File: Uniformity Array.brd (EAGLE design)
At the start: 43.2 x 34.3 mm, 38 parts, among them IC1 SI1145, J3 USB-MICRO!!!, J4 3x2M, Q1 200mA/50V, Q2 200mA/50V, U1 ATMEGA32U4-TQFP44, U2 ATMEGA32U4-TQFP44, U4 LP2985-33DBVR, Y3 16MHz KX-7

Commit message: schematiced
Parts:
- removed C8: 1uF, SmartPrj:C0402
- removed IC1: SI1145, silabs:QFN-10
- removed L2: MH2029-300Y, wuerth-elektronik:0805
- removed Q1, Q2: 200mA/50V, SparkFun-DiscreteSemi:SOT23-3
- removed R3, R6, R9: (no value), arduino-micro-reference-designArduino_Micro_Rev03j:SMARTPRJ_R0402
- removed R7: (no value), arduino-micro-reference-designArduino_Micro_Rev03j:SMARTPRJ_R0603-ROUND
- removed RESET: TS42, SmartPrj:TS42
- removed RP3: 22R, resistor-dil:CAY16
- removed Y3: 16MHz KX-7, SmartPrj:CRYSTAL-3.2-2.5
- added C1, C15, C16, C17, C18, C19, C2, C20, C21, C22, C23, C24, C25, C26, C27, C28, C29, C3, C30, C31, C32, C33, C34: 1uf, Seeed-Capacitor-2016:C0402
- added IC10, IC11, IC12, IC13, IC14, IC15, IC16, IC17, IC18, IC19, IC2, IC20, IC21, IC3, IC4, IC5, IC6, IC7, IC8, IC9: SI1145, silabs:QFN-10
- added K1: DTSM-62K-S-V-T/R, Seeed-Switch-2016:SW4-SMD-6.0X6.0X5.0MM
- added L1: 330R-1500MA, Seeed-OPL-Inductor:L0805
- added R10: 10K, Seeed-OPL-Resistor:R0402
- added R11: 22R, Seeed-Resistor-2016:R0603
- added R12, R13, R14, R15, R16, R17, R18, R19, R20, R21, R22, R23, R24, R25, R26, R27, R28, R29, R30, R31, R32, R33, R34, R35, R36, R37, R38, R39, R40, R41, R42, R43, R44, R45, R46, R47, R48, R49, R50, R51, R52, R53: 510R, Seeed-Resistor-2016:R0603
- added U3, U5: PCA9547D,112, NXP_By_element14_Batch_1:SOIC127P1032X265-24N
- added Y1: 16MHZ, Seeed-Crystal Oscillator-2016:X2-SMD-5.0X3.2X1.3MM
- C10, C11, C6, C9: value 100n -> 100nf; device SmartPrj:C0402 -> Seeed-Capacitor-2016:C0402
- C12: value 22pF -> 10pf; device SmartPrj:C0402 -> Seeed-Capacitor-2016:C0603
- C13: value 22pF -> 4.7PF; device SmartPrj:C0402 -> Seeed-Capacitor-2016:C0603
- C14: value 22u -> 22uf; device rcl:SMC_B -> Seeed-Capacitor-2016:AVX-A
- C4, C7: value 1uF -> 1uf; device SmartPrj:C0402 -> Seeed-Capacitor-2016:C0402
- C5: value 1uF -> 1uf; device arduino-micro-reference-designArduino_Micro_Rev03j:SMARTPRJ_C0603-ROUND -> Seeed-Capacitor-2016:C0402
- D2: value CD1206-S01575 -> 75V 150MA; device diode:MINIMELF -> Seeed-Diode-2016:LED-1206
- F1: value MF-MSMF050-2 500mA -> MF-MSMF050-2; device rcl:L1812 -> Seeed-Fuse-2016:F1812
- J4: value 3x2M -> 2x3p-2.54; device SmartPrj:2X03 -> Seeed-Connector -2016:H2X3-2.54
- L: value green -> GREEN-0805; device led:CHIPLED_0805 -> Seeed-LED-2016:LED-0805
- ON: value blue -> CLEAR-BLUE-0805; device led:CHIPLED_0805 -> Seeed-LED-2016:LED-0805
- R1, R2, R5, R8: device SmartPrj:R0402 -> Seeed-Resistor-2016:R0402
- R4: value 10K -> 22R; device SmartPrj:R0402 -> Seeed-Resistor-2016:R0603
- U2: value ATMEGA32U4-TQFP44 -> PCA9547D,112; device Seeed-OPL-ic:TQFP44-0.8-9.6X9.6MM -> NXP_By_element14_Batch_1:SOIC127P1032X265-24N
- U4: device SmartPrj:SOT23-DBV -> Seeed-IC-2016:SOT-23-5
- Z1, Z2: value CG0603MLC-05E -> 5V-28V; device varistor:CT/CN0603 -> Seeed-Diode-2016:R0603
- moved U2 65.1 mm to (52.1, 26.7), turned to 90 degrees
- moved R4 57.5 mm to (-6.35, -22.9), turned to 0 degrees
- moved U4 6.35 mm to (27.9, 33.0)
- moved C11 5.08 mm to (24.1, 29.2)
- moved R2 3.81 mm to (15.2, 31.8)
- moved R5 3.81 mm to (15.2, 34.3)
- moved ON 2.84 mm to (19.8, 33.4)
- moved C14 2.54 mm to (3.81, 30.9)
- moved C4 2.54 mm to (31.8, 29.2)
- moved C6 2.54 mm to (20.3, 27.7)
- moved C7 2.54 mm to (17.8, 27.7)
- moved C9 2.54 mm to (17.8, 30.5)
- moved F1 2.54 mm to (9.65, 31.0)
- moved U1 1.27 mm to (21.6, 20.3)
- moved J4 0.28 mm to (13.8, 9.65), turned to 90 degrees
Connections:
- removed net 5-GND: RESET.5
- removed net HWB: R4.1, U1.33
- removed net N$2: IC1.1, Q1.2, R3.1
- removed net N$4: IC1.2, Q2.2, R6.1
- new net N$10: IC8.1, R13.2, U2.4
- new net N$11: IC8.2, R35.2, U2.5
- new net N$12: IC3.1, R18.2, U2.15
- new net N$13: IC4.1, R19.2, U2.13
- new net N$14: IC4.2, R21.2, U2.14
- new net N$15: IC3.2, R20.2, U2.16
- new net N$16: IC9.1, R17.2, U2.8
- new net N$17: IC9.2, R15.2, U2.9
- new net N$18: IC6.1, R16.2, U2.10
- new net N$19: IC6.2, R14.2, U2.11
- new net N$20: IC5.1, R45.2, U2.17
- new net N$21: IC5.2, R47.2, U2.18
- new net N$22: IC2.1, R46.2, U2.20
- new net N$23: IC2.2, R44.2, U2.19
- new net N$24: IC11.1, R24.2, U5.6
- new net N$25: IC12.1, R25.2, U5.4
- new net N$26: IC12.2, R23.2, U5.5
- new net N$27: IC11.2, R22.2, U5.7
- new net N$28: IC13.1, R27.2, U5.8
- new net N$29: IC13.2, R29.2, U5.9
- new net N$30: IC10.1, R26.2, U5.10
- new net N$31: IC10.2, R28.2, U5.11
- new net N$32: IC15.1, R30.2, U5.15
- new net N$33: IC16.1, R31.2, U5.13
- new net N$34: IC16.2, R33.2, U5.14
- new net N$35: IC15.2, R32.2, U5.16
- new net N$36: IC17.1, R50.2, U5.17
- new net N$37: IC17.2, R48.2, U5.18
- new net N$38: IC14.1, R51.2, U5.19
- new net N$39: IC14.2, R49.2, U5.20
- new net N$40: IC19.1, R38.2, U3.6
- new net N$41: IC20.1, R39.2, U3.4
- new net N$42: IC20.2, R37.2, U3.5
- new net N$43: IC19.2, R36.2, U3.7
- new net N$44: IC21.1, R41.2, U3.8
- new net N$45: IC21.2, R43.2, U3.9
- new net N$46: IC18.1, R40.2, U3.10
- new net N$47: IC18.2, R42.2, U3.11
- new net N$52: U5.3
- new net N$53: U3.3
- new net N$59: U2.3
- new net N$6: R10.2, U1.33
- new net N$8: IC7.1, R12.2, U2.6
- new net N$9: IC7.2, R34.2, U2.7
- net 3V3: now also C15.1, C17.1, C18.1, C19.1, C2.1, C21.1, C22.1, C23.1, C25.1, C26.1, C27.1, C29.1, C3.1, C30.1, C31.1, C32.2, C33.2, C34.2, IC10.3, IC11.3, IC12.3, IC13.3, IC14.3, IC15.3, IC16.3, IC17.3, IC18.3, IC19.3, IC2.3, IC20.3, IC21.3, IC3.3, IC4.3, IC5.3, IC6.3, IC7.3, IC8.3, IC9.3, R12.1, R13.1, R14.1, R15.1, R16.1, R17.1, R18.1, R19.1, R20.1, R21.1, R22.1, R23.1, R24.1, R25.1, R26.1, R27.1, R28.1, R29.1, R30.1, R31.1, R32.1, R33.1, R34.1, R35.1, R36.1, R37.1, R38.1, R39.1, R40.1, R41.1, R42.1, R43.1, R44.1, R45.1, R46.1, R47.1, R48.1, R49.1, R50.1, R51.1, U2.24, U3.2, U3.24, U5.1, U5.24; no longer C8.1, IC1.3, Q1.1, Q2.1, R3.2, R6.2
- net A3: no longer U1.39
- net AVCC: now also L1.1; no longer L2.2
- net D+: now also R4.1; no longer RP3.8
- net D-: now also R11.1; no longer RP3.7
- net GND: now also C1.2, C15.2, C16.2, C17.2, C18.2, C19.2, C2.2, C20.2, C21.2, C22.2, C23.2, C24.2, C25.2, C26.2, C27.2, C28.2, C29.2, C3.2, C30.2, C31.2, C32.1, C33.1, C34.1, IC10.8, IC11.8, IC12.8, IC13.8, IC14.8, IC15.8, IC16.8, IC17.8, IC18.8, IC19.8, IC2.8, IC20.8, IC21.8, IC3.8, IC4.8, IC5.8, IC6.8, IC7.8, IC8.8, IC9.8, J4.4, K1.2, K1.3, L.-, ON.-, R10.1, U2.1, U2.12, U2.2, U2.21, U3.1, U3.12, U3.21, U5.12, U5.2, U5.21; no longer C8.2, IC1.8, J4.6, L.C, ON.C, R4.2, RESET.3, RESET.4, Y3.2, Y3.4
- net MOSI: now also J4.5; no longer J4.4
- net N$3: now also ON.+; no longer ON.A
- net N$7: now also L.+; no longer L.A
- net RD+: now also R4.2; no longer RP3.1
- net RD-: now also R11.2; no longer RP3.2
- net RESET: now also D2.+, J4.3, K1.4; no longer D2.A, J4.5, RESET.2
- net SCK: now also J4.2; no longer J4.3
- net SCL: now also R53.1, U2.22, U3.22, U5.22; no longer Q2.3, R7.1
- net SDA: now also R52.1, U2.23, U3.23, U5.23; no longer Q1.3, R9.1
- net VUSB: now also D2.-, J4.6, L1.2, R52.2, R53.2; no longer D2.C, J4.2, L2.1, R7.2, R9.2
- net XTAL1: now also Y1.2; no longer Y3.3
- net XTAL2: now also Y1.1; no longer Y3.1
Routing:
- net GND: track 95.6 -> 5.07 mm, vias 11 -> 0
- net VUSB: track 84.2 -> 0.00 mm, vias 2 -> 0
- net 3V3: track 38.5 -> 0.00 mm
- net RESET: track 28.2 -> 0.00 mm
- net SCL: track 15.0 -> 0.00 mm
- net SDA: track 14.0 -> 0.00 mm
- net VUSBD: track 12.6 -> 0.00 mm
- net MOSI: track 11.9 -> 0.00 mm
- net MISO: track 8.95 -> 0.00 mm
- net SCK: track 8.86 -> 0.00 mm
- net D+: track 7.77 -> 0.00 mm
- net N$4: track 7.74 -> 0.00 mm
- net D-: track 7.55 -> 0.00 mm
- net XTAL1: track 7.36 -> 0.00 mm
- net AVCC: track 6.68 -> 0.00 mm
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- removed copper zone on layer 16, net GND
- removed copper zone on layer 1, net N$5
- removed copper zone on layer 1, net VUSB
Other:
- board outline removed

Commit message: sensors placed
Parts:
- moved C32 523.3 mm to (91.4, 69.8)
- moved C33 510.3 mm to (66.0, 69.8)
- moved C34 500.9 mm to (45.7, 69.8)
- moved R52 492.8 mm to (25.4, 69.8)
- moved R53 492.8 mm to (20.3, 69.8)
- moved R50 469.3 mm to (77.5, 17.8), turned to 180 degrees
- moved R51 469.0 mm to (77.5, 12.7), turned to 180 degrees
- moved R42 466.9 mm to (90.2, 39.4)
- moved R43 466.9 mm to (90.2, 34.3)
- moved R48 454.9 mm to (77.5, 7.62), turned to 180 degrees
- moved R49 454.6 mm to (77.5, 2.54), turned to 180 degrees
- moved R40 451.3 mm to (90.2, 29.2)
- moved R41 451.3 mm to (90.2, 24.1)
- moved R44 434.3 mm to (53.3, 17.8), turned to 180 degrees
- moved R45 433.4 mm to (53.3, 12.7), turned to 180 degrees
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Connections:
- net 3V3: now also C1.1, C20.1, C24.1, C28.1
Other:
- board outline added: 102.9 x 81.3 mm

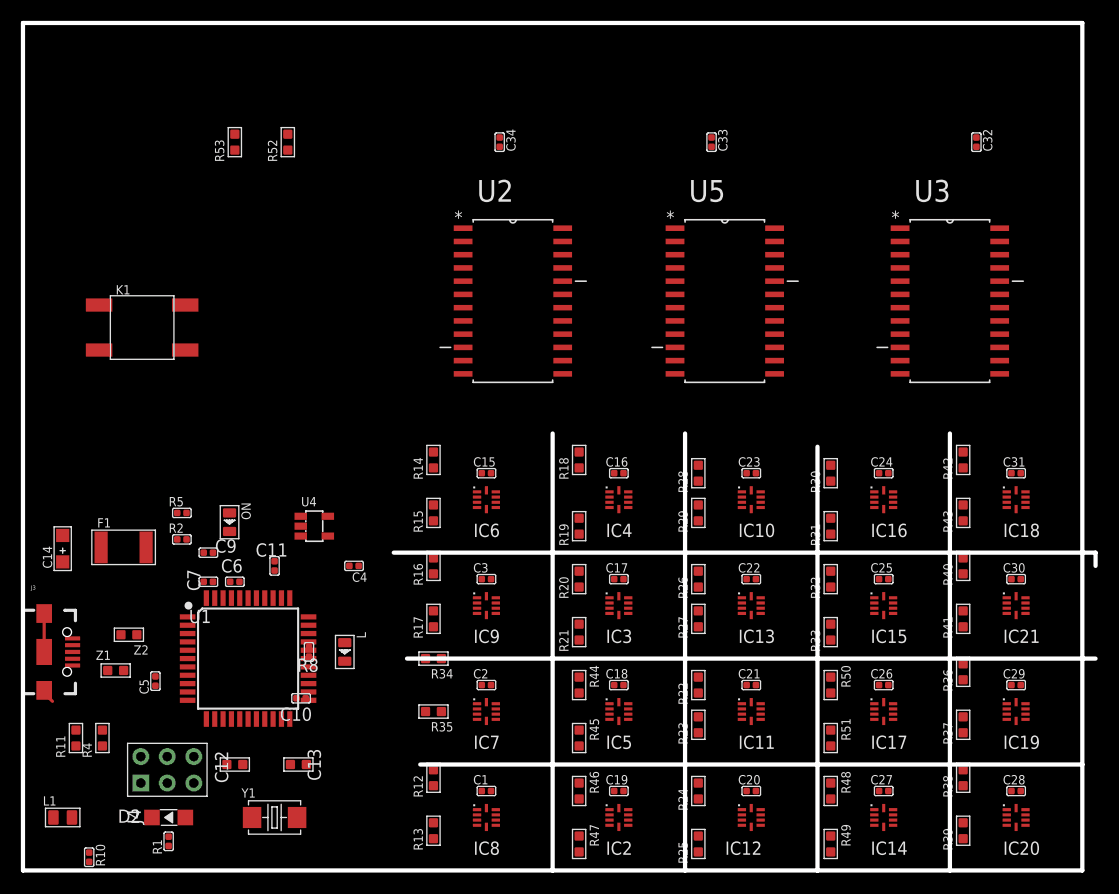
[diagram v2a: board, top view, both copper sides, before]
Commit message: routed the sensors
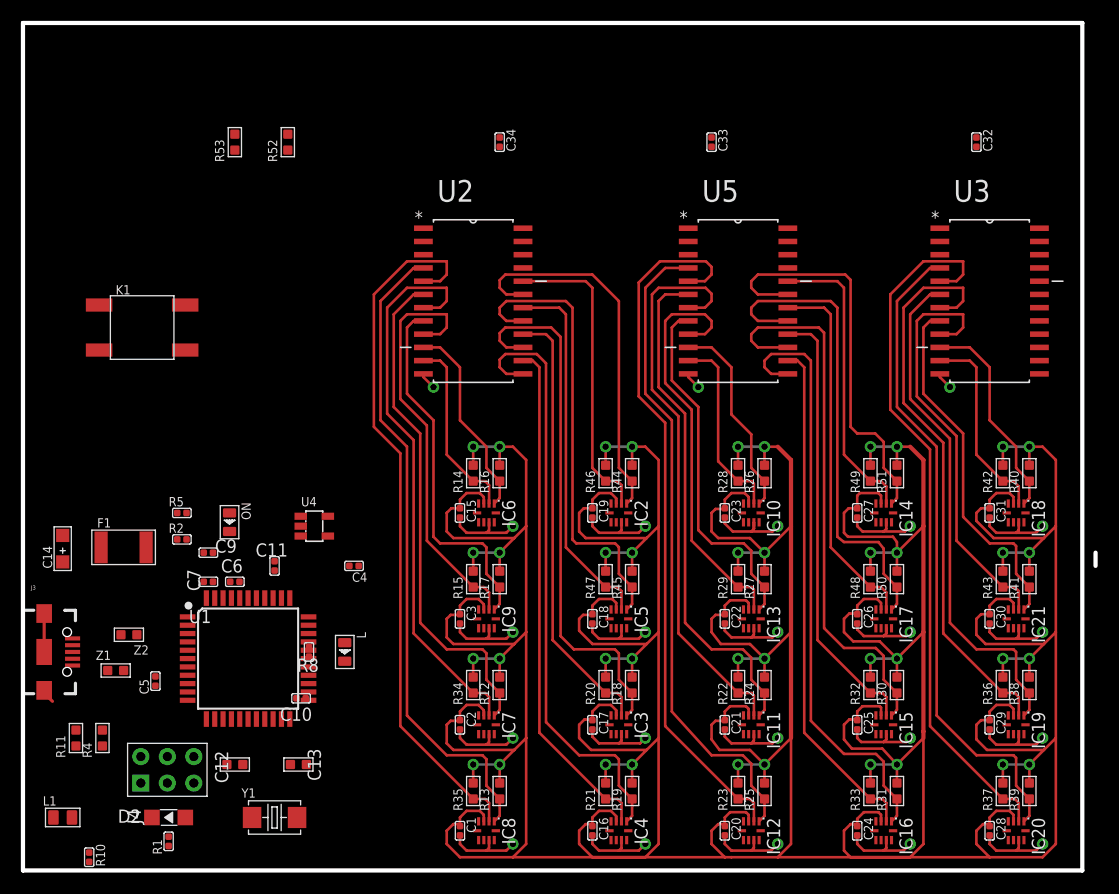
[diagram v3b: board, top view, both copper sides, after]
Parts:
- moved R49 35.8 mm to (81.3, 38.1), turned to 0 degrees
- moved C16 34.4 mm to (54.6, 3.81), turned to 0 degrees
- moved C24 34.4 mm to (80.0, 3.81), turned to 0 degrees
- moved IC16 31.8 mm to (82.5, 3.81), turned to 270 degrees
- moved IC4 31.8 mm to (57.1, 3.81), turned to 270 degrees
- moved R46 30.6 mm to (55.9, 38.1), turned to 0 degrees
- moved IC14 29.2 mm to (82.5, 34.3), turned to 270 degrees
- moved IC2 29.2 mm to (57.1, 34.3), turned to 270 degrees
- moved C19 26.8 mm to (54.6, 34.3), turned to 0 degrees
- moved C27 26.8 mm to (80.0, 34.3), turned to 0 degrees
- moved R31 26.2 mm to (83.8, 7.62)
- moved R51 26.2 mm to (83.8, 38.1), turned to 0 degrees
- moved R19 25.9 mm to (58.4, 7.62)
- moved R47 25.5 mm to (55.9, 27.9), turned to 0 degrees
- moved R18 22.2 mm to (58.4, 17.8)
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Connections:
- removed net N$22: IC2.1, R46.2, U2.20
- removed net N$23: IC2.2, R44.2, U2.19
- new net N$20: IC2.1, R44.2, U2.19
- new net N$21: IC2.2, R46.2, U2.20
- net 3V3: now also C16.1
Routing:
- net 3V3: track 0.00 -> 700.1 mm, vias 0 -> 40
- net GND: track 5.07 -> 159.3 mm, vias 0 -> 23
- net N$42: track 0.00 -> 68.4 mm
- net N$26: track 0.00 -> 68.2 mm
- net N$11: track 0.00 -> 67.9 mm
- net N$41: track 0.00 -> 62.9 mm
- net N$25: track 0.00 -> 62.7 mm
- net N$10: track 0.00 -> 62.3 mm
- net N$13: track 0.00 -> 57.8 mm
- net N$33: track 0.00 -> 57.7 mm
- net N$43: track 0.00 -> 54.6 mm
- net N$27: track 0.00 -> 54.6 mm
- net N$9: track 0.00 -> 54.1 mm
- net N$32: track 0.00 -> 53.4 mm
- net N$12: track 0.00 -> 51.3 mm
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- added copper zone on layer 16, net GND
- added copper zone on layer 16, net N$4
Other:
- outline, holes or cut-outs redrawn

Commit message: routed! (also pulled ~RESET hight)
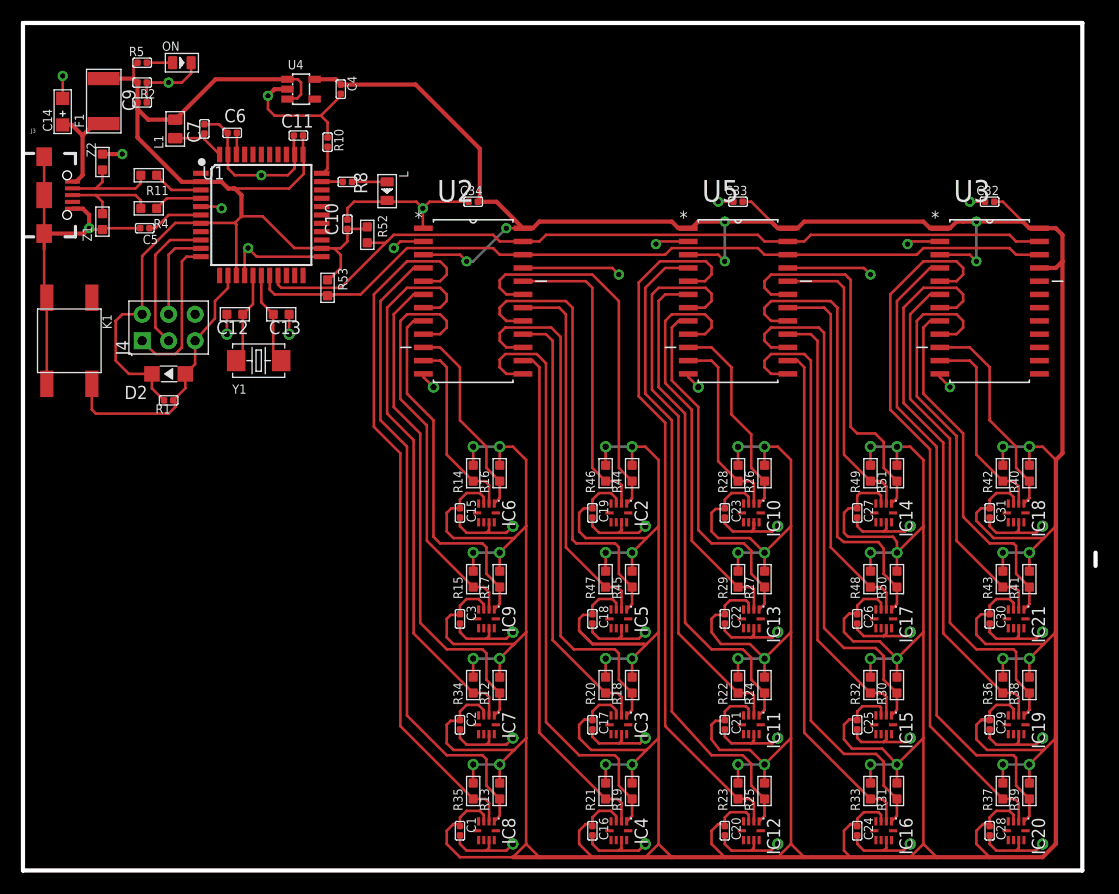
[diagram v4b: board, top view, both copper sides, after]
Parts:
- moved R10 72.3 mm to (29.2, 69.8)
- moved L1 66.9 mm to (14.6, 71.1), turned to 90 degrees
- moved R11 54.4 mm to (12.1, 66.7), turned to 90 degrees
- moved R4 51.0 mm to (12.1, 63.5), turned to 90 degrees
- moved C4 45.7 mm to (30.5, 74.9), turned to 0 degrees
- moved C10 45.7 mm to (31.1, 62.0), turned to 180 degrees
- moved Z2 45.4 mm to (7.62, 67.9), turned to 180 degrees
- moved R8 45.2 mm to (31.1, 66.0), turned to 90 degrees
- moved L 44.4 mm to (34.9, 65.2)
- moved ON 44.3 mm to (15.2, 77.5), turned to 0 degrees
- moved R2 44.0 mm to (11.4, 75.6), turned to 270 degrees
- moved Y1 43.8 mm to (22.6, 48.9)
- moved J3 43.8 mm to (2.03, 64.8)
- moved C9 43.6 mm to (11.4, 73.7), turned to 90 degrees
- moved C5 43.4 mm to (11.7, 61.6), turned to 270 degrees
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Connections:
- removed net N$52: U5.3
- removed net N$53: U3.3
- removed net N$59: U2.3
- net 3V3: now also U2.3, U3.1, U3.21, U3.3, U5.3; no longer U3.2
- net GND: now also U3.2; no longer U3.1, U3.21
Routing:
- net 3V3: track 700.1 -> 855.8 mm, vias 40 -> 46
- net GND: track 159.3 -> 294.0 mm, vias 23 -> 41
- net VUSB: track 0.00 -> 110.4 mm
- net SDA: track 0.00 -> 79.2 mm
- net SCL: track 0.00 -> 79.2 mm
- net RESET: track 0.00 -> 25.7 mm
- net MISO: track 0.00 -> 14.9 mm
- net SCK: track 0.00 -> 13.7 mm
- net VUSBD: track 0.00 -> 9.85 mm
- net XTAL2: track 0.00 -> 9.58 mm
- net D-: track 0.00 -> 9.57 mm
- net D+: track 0.00 -> 9.56 mm
- net MOSI: track 0.00 -> 9.06 mm
- net XTAL1: track 0.00 -> 8.96 mm
- net AVCC: track 0.00 -> 5.59 mm
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- added copper zone on layer 1, net 3V3

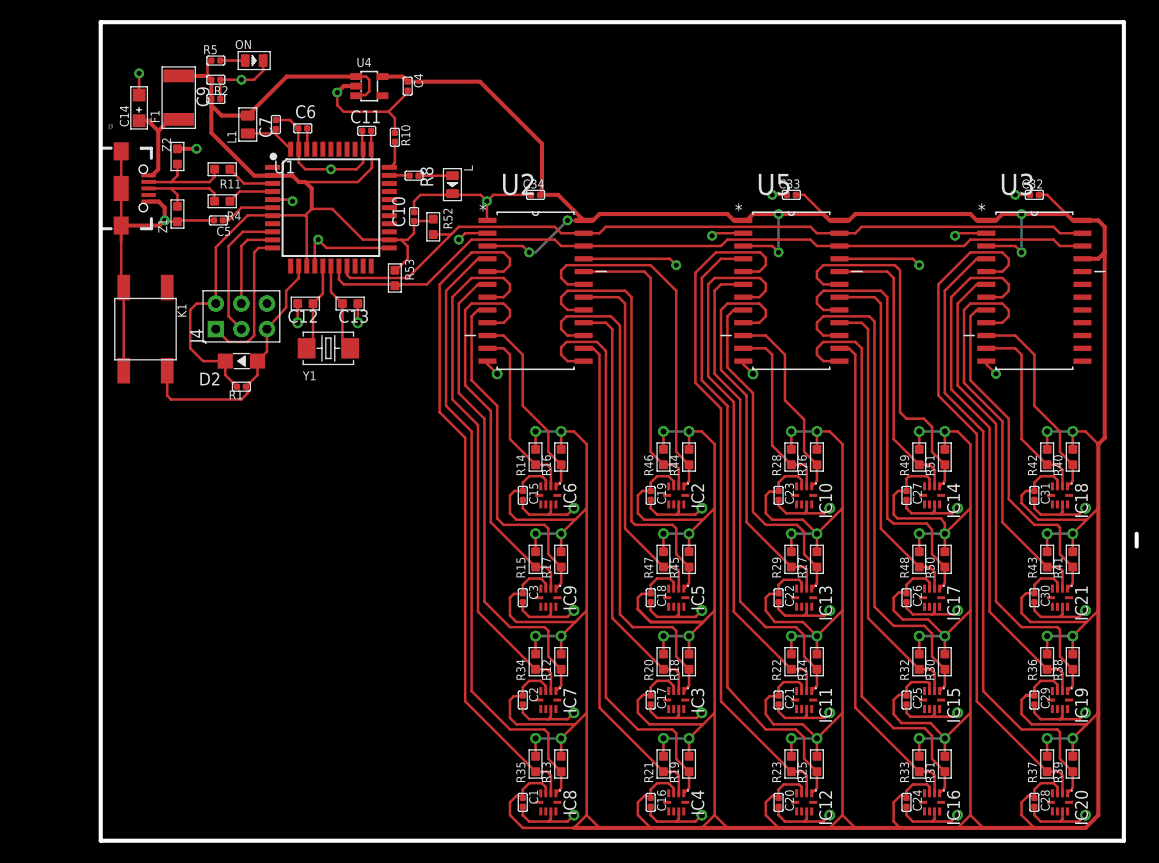
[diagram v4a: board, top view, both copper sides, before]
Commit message: replaced USB, gerbered, BOM
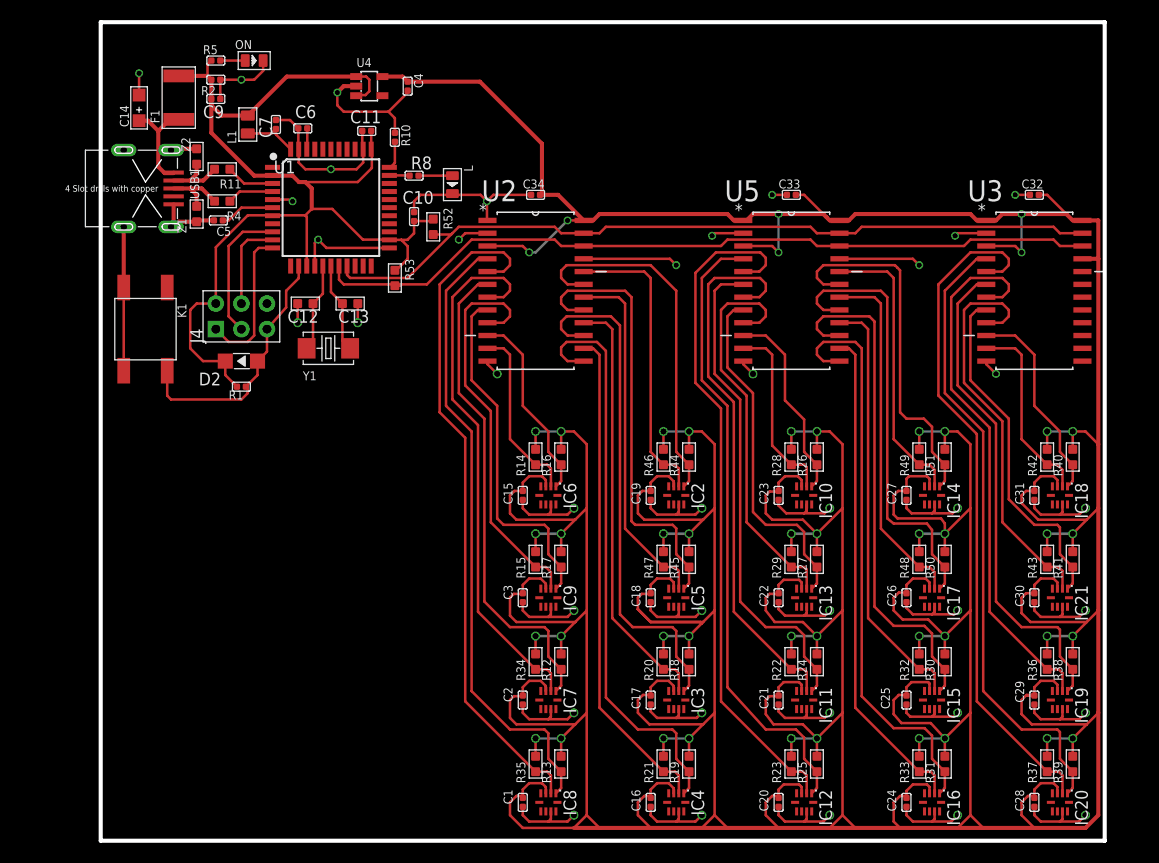
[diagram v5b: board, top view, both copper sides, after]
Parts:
- removed J3: USB-MICRO!!!, SparkFun-Connectors:USB-B-MICRO-SMD_V03
- added USB1: ST-USB-013A, Seeed-Connector -2016:MINIUSB5+4P-0.8-90D
- moved Z1 1.91 mm to (9.53, 62.2)
- moved Z2 1.91 mm to (9.53, 67.9)
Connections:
- net D+: now also USB1.3; no longer J3.D+
- net D-: now also USB1.2; no longer J3.D-
- net GND: now also USB1.5, USB1.GND@1, USB1.GND@2, USB1.GND@3, USB1.GND@4; no longer J3.GND, J3.SHIELD1, J3.SHIELD2, J3.SHIELD3
- net VUSBD: now also USB1.1; no longer J3.VBUS
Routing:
- net GND: track 294.0 -> 280.6 mm, vias 41 -> 39
- net D-: track 9.57 -> 6.42 mm
- net D+: track 9.56 -> 6.63 mm
- net 3V3: track 855.8 -> 854.4 mm
- removed copper zone on layer 16, net N$4
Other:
- board size 102.9 x 81.3 mm -> 99.7 x 81.3 mm
